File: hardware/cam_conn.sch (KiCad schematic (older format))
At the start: 1 part, among them J1901 LSHM-150-xxx-x-DV-A-S

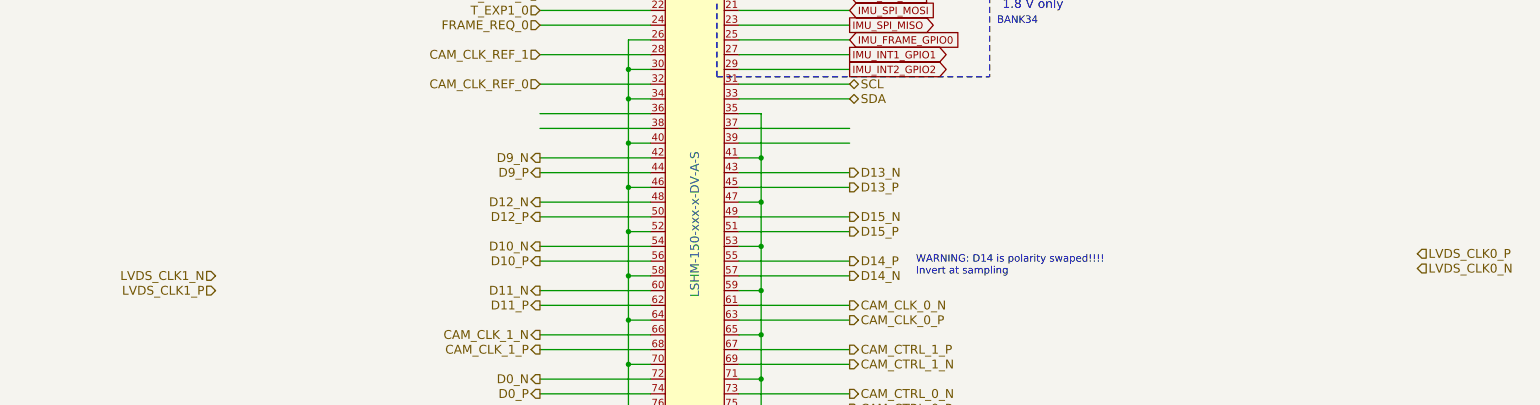
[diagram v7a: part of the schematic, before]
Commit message: general routing mainly power distribution, fixed some footprints
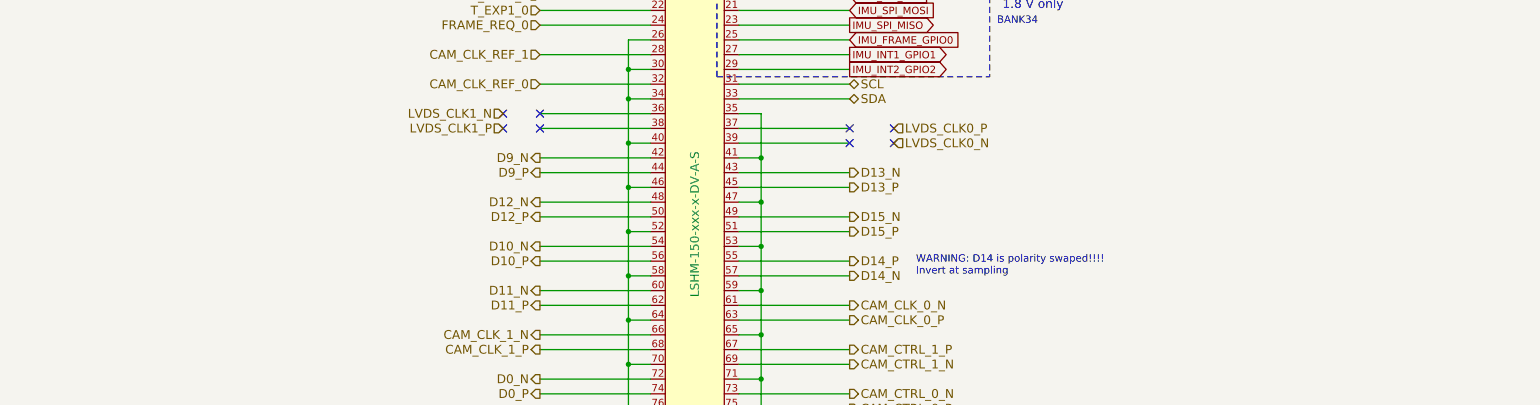
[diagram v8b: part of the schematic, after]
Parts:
- J1901: footprint Connectors_Samtec:LSHM-150-xxx-x-DV-A-S -> Connector_Samtec:Samtec_LSHM-150-xx.x-x-DV-S_2x50-1SH_P0.50mm_Vertical
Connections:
- no-connect marks 0 -> 8
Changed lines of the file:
@@
 $Descr A4 11693 8268
 encoding utf-8
-Sheet 19 21
+Sheet 18 21
 Title ""
 Date ""
@@
 F 0 "J1901" H 8350 850 60  0000 C CNN
 F 1 "LSHM-150-xxx-x-DV-A-S" V 8350 3400 60  0000 C CNN
-F 2 "Connectors_Samtec:LSHM-150-xxx-x-DV-A-S" H 8350 4550 60  0001 C CNN
+F 2 "Connector_Samtec:Samtec_LSHM-150-xx.x-x-DV-S_2x50-1SH_P0.50mm_Vertical" H 8350 4550 60  0001 C CNN
 F 3 "http://suddendocs.samtec.com/catalog_english/lshm_dv.pdf" H 8350 4550 60  0001 C CNN
 F 4 "Samtech" H 8350 3400 60  0001 C CNN "MFG Name"
@@
 Text HLabel 7300 2250 0    60   Input ~ 0
 CAM_CLK_REF_1
-Text HLabel 13250 3700 2    60   Input ~ 0
+Text HLabel 9700 2850 2    60   Input ~ 0
 LVDS_CLK0_N
-Text HLabel 13250 3600 2    60   Input ~ 0
+Text HLabel 9700 2750 2    60   Input ~ 0
 LVDS_CLK0_P
-Text HLabel 5100 3750 0    60   Input ~ 0
+Text HLabel 7050 2650 0    60   Input ~ 0
 LVDS_CLK1_N
-Text HLabel 5100 3850 0    60   Input ~ 0
+Text HLabel 7050 2750 0    60   Input ~ 0
 LVDS_CLK1_P
 Wire Wire Line
@@
 Text Notes 10400 2050 0    50   ~ 0
 BANK34
+NoConn ~ 7300 2650
+NoConn ~ 7300 2750
+NoConn ~ 9400 2750
+NoConn ~ 9400 2850
+NoConn ~ 7050 2650
+NoConn ~ 7050 2750
+NoConn ~ 9700 2750
+NoConn ~ 9700 2850
 $EndSCHEMATC
